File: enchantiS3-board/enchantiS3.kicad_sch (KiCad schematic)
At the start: 61 parts, among them J1 USB_C_Receptacle_USB2.0, SW1 B3U-1000P, SW2 B3U-1000P, U1 USBLC6-2P6, U11 MAX17262REWL+T, U12 BQ25185DLHR, U13 ICM-42670-P, U2 MMC5633NJL, U4 NCP167AMX330TBG, U9 NCP167AMX330TBG

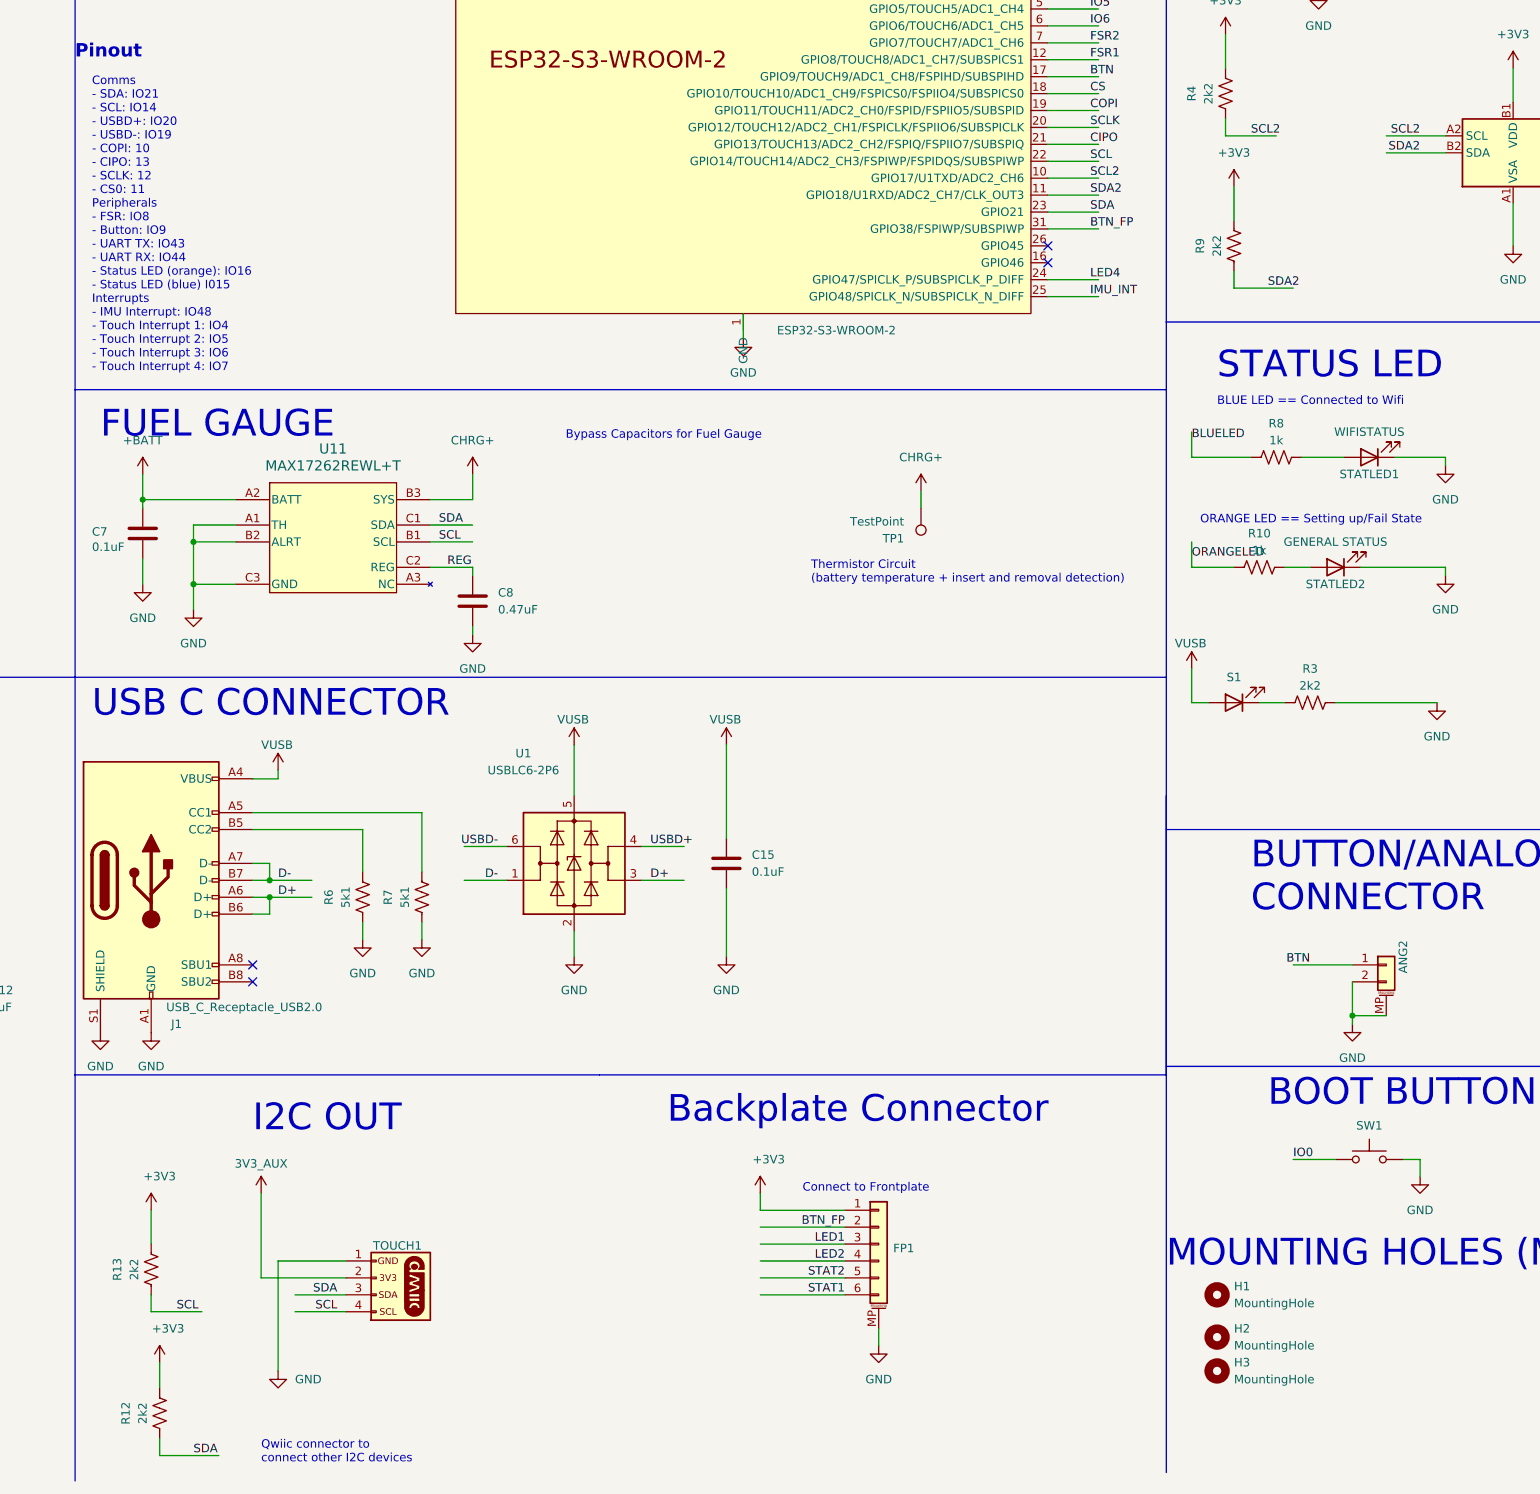
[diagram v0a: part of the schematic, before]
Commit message: fixed hole size constraints for pcbway manufacturing, updated frontplate connector,
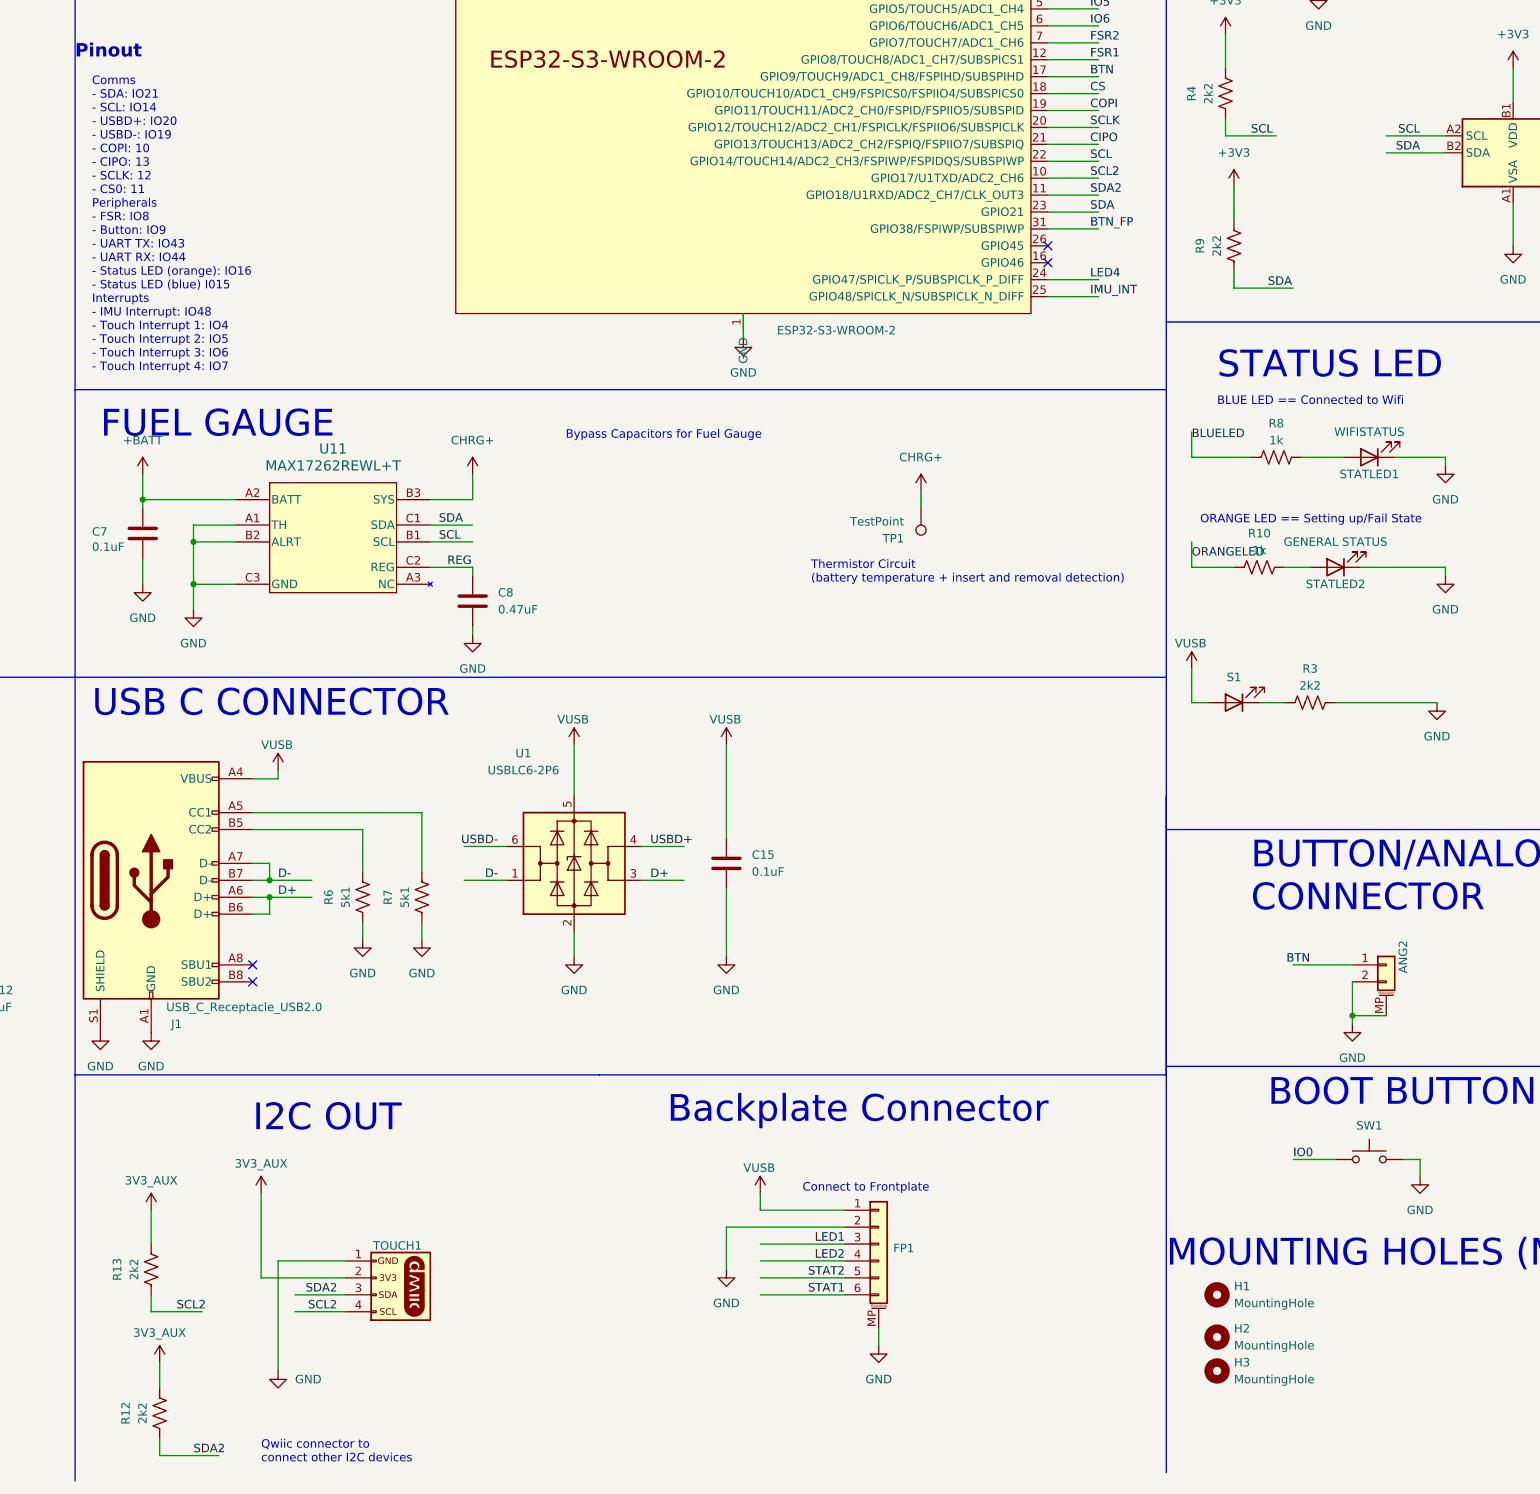
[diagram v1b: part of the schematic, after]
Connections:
- net +3V3: no longer FP1.1 (Pin_1), R12.2, R13.2
- net 3V3_AUX: now also R12.2, R13.2
- net BTN_FP: no longer FP1.2 (Pin_2)
- net GND: now also FP1.2 (Pin_2)
- net SCL: now also R4.1, U2.A2 (SCL); no longer R13.1, TOUCH1.4 (SCL)
- net SCL2: now also R13.1, TOUCH1.4 (SCL); no longer R4.1, U2.A2 (SCL)
- net SDA: now also R9.1, U2.B2 (SDA); no longer R12.1, TOUCH1.3 (SDA)
- net SDA2: now also R12.1, TOUCH1.3 (SDA); no longer R9.1, U2.B2 (SDA)
- net VUSB: now also FP1.1 (Pin_1)

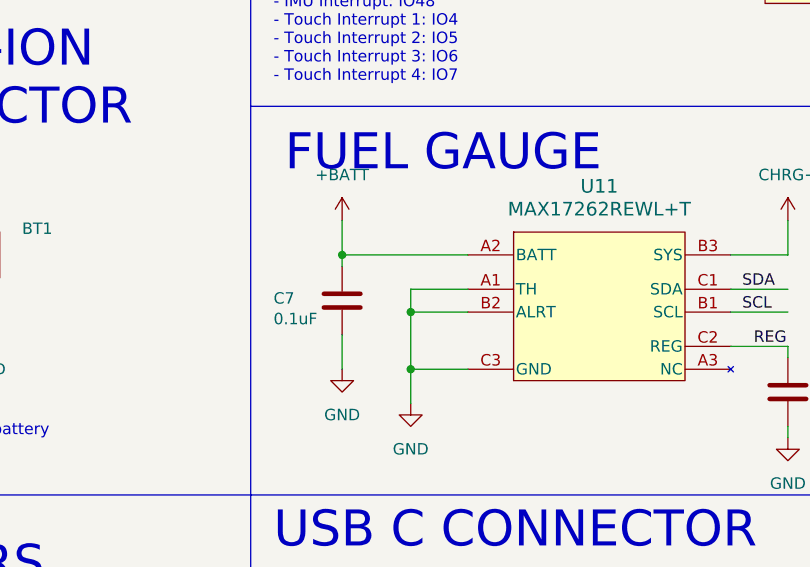
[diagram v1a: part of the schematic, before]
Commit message: add sensor fusion testing firmware
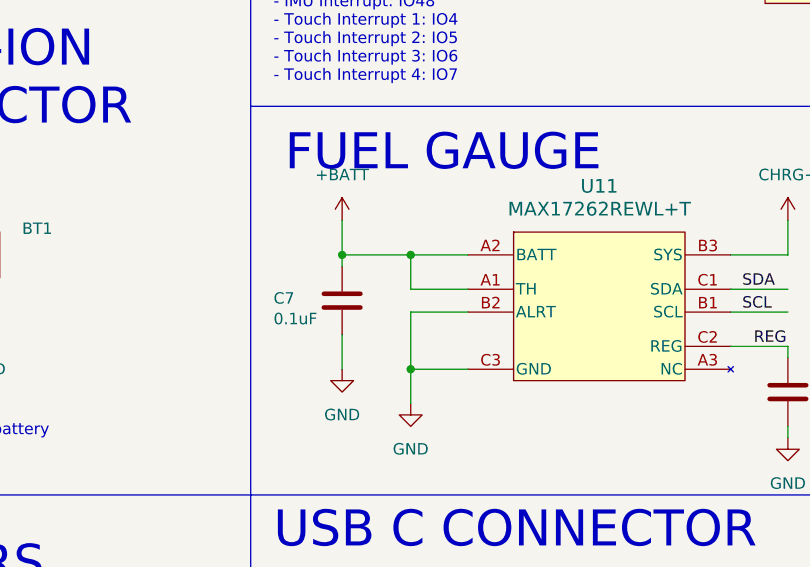
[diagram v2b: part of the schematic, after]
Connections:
- net +BATT: now also U11.A1 (TH)
- net GND: no longer U11.A1 (TH)
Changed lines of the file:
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@@
+	)
+	(junction
+		(at 128.27 137.16)
+		(diameter 0)
+		(color 0 0 0 0)
 	)
 	(junction
 		(at 368.3 214.63)
-		(diameter 0)
-		(color 0 0 0 0)
-	)
-	(junction
-		(at 128.27 143.51)
 		(diameter 0)
 		(color 0 0 0 0)
@@
 	(wire
 		(pts
-			(xy 128.27 140.97) (xy 128.27 143.51)
-		)
-		(stroke
-			(width 0)
-			(type default)
-		)
-	)
-	(wire
-		(pts
 			(xy 391.16 204.47) (xy 392.43 204.47)
 		)
@@
 	(wire
 		(pts
+			(xy 128.27 137.16) (xy 120.65 137.16)
+		)
+		(stroke
+			(width 0)
+			(type default)
+		)
+	)
+	(wire
+		(pts
 			(xy 278.13 127) (xy 278.13 130.81)
 		)
@@
 	(wire
 		(pts
+			(xy 128.27 140.97) (xy 128.27 137.16)
+		)
+		(stroke
+			(width 0)
+			(type default)
+		)
+	)
+	(wire
+		(pts
 			(xy 391.16 214.63) (xy 397.51 214.63)
 		)
@@
 	(wire
 		(pts
-			(xy 134.62 137.16) (xy 120.65 137.16)
+			(xy 134.62 137.16) (xy 128.27 137.16)
 		)
 		(stroke
@@
 	(wire
 		(pts
-			(xy 128.27 140.97) (xy 134.62 140.97)
-		)
-		(stroke
-			(width 0)
-			(type default)
-		)
-	)
-	(wire
-		(pts
 			(xy 123.19 278.13) (xy 123.19 280.67)
 		)
 		(stroke
+			(width 0)
+			(type default)
+		)
+	)
+	(wire
+		(pts
+			(xy 134.62 140.97) (xy 128.27 140.97)
+		)
+		(stroke

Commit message: added capsense controller on enchantiS3 board
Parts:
- removed ANG2: CONN HEADER SMD 2POS 1MM, ENCHANTI_connectors:Molex_Pico-Clasp_2pin_Vertical, symbol ENCHANTI_connectors:PicoClasp_2pin
- removed BOARDLAYOUT1: LAYOUT, pin-layout:board-layout, symbol pin-layout:board-layout
- removed CHARGLED1: S1, LED_SMD:LED_0402_1005Metric, symbol Device:LED
- removed FP1: CONN HEADER SMD 6POS 1MM, ENCHANTI_connectors:Molex_Pico-Clasp_501331-0607_1x06-1MP_P1.00mm_Vertical, symbol Connector_Generic_MountingPin:Conn_01x06_MountingPin
- removed R10: 1k, Resistor_SMD:R_0402_1005Metric, symbol Device:R_US
- removed R3, R4, R9: 2k2, Resistor_SMD:R_0402_1005Metric, symbol Device:R_US
- removed STATLED1: WIFISTATUS, LED_SMD:LED_0402_1005Metric, symbol Device:LED
- removed STATLED2: GENERAL STATUS, LED_SMD:LED_0402_1005Metric, symbol Device:LED
- removed SW1, SW2: B3U-1000P, Button_Switch_SMD:SW_SPST_B3U-1000P, symbol Switch:SW_Push
- removed SYS2: SYS, symbol power-symbols:VSYS
- removed U11: MAX17262REWL+T, ENCHANTI_battery-management:MAX17262, symbol ENCHANTI_battery-management:MAX17262REWL+T
- removed U2: MMC5633NJL, Package_BGA:WLP-4_0.86x0.86mm_P0.4mm, symbol Sensor_Magnetic:MMC5633NJL
- added C10, C26, C59: 1uF, Capacitor_SMD:C_0402_1005Metric, symbol Device:C
- added C14, C27, C6, C61, C66: 0.1uF, Capacitor_SMD:C_0402_1005Metric, symbol Device:C
- added C16, C20, C24, C25: 2.2nF, Capacitor_SMD:C_0402_1005Metric, symbol Device:C
- added CHARGLED2: RED_LED, LED_SMD:LED_0603_1608Metric, symbol Device:LED
- added CHARGLED3: YELLOW_LED, LED_SMD:LED_0603_1608Metric, symbol Device:LED
- added D2: NUP2105L, Package_TO_SOT_SMD:SOT-23, symbol Power_Protection:NUP2105L
- added FP1: CONN HEADER SMD 6POS 1MM, Connector_Molex:Molex_Pico-Clasp_501331-0607_1x06-1MP_P1.00mm_Vertical, symbol ENCHANTI_connectors:PicoClasp_6pin
- added J2: Programming Header, ENCHANTI_connectors:SAMTEC_FTSH-105-01-F-DV-P-TR, symbol ENCHANTI_connectors:Programming_Header
- added R14, R16: 2k2, Resistor_SMD:R_0402_1005Metric, symbol Device:R_US
- added R19: 120, Resistor_SMD:R_0402_1005Metric, symbol Device:R_US
- added R3: 5mOhm, ENCHANTI_resistors:WSTC080R003_20, symbol ENCHANTI_resistors:WSTC0805DLR005FNR
- added R42, R43: 604R, Resistor_SMD:R_0402_1005Metric, symbol Device:R_US
- added R50: 261, Resistor_SMD:R_0402_1005Metric, symbol Device:R_US
- added R51: 549, Resistor_SMD:R_0402_1005Metric, symbol Device:R_US
- added SW1, SW2, SW3: PTS810, ENCHANTI_switches:SW_SPST_PTS810, symbol ENCHANTI_switches:PTS810
- added TOUCH2: FFCHEADER, ffc_footprints:CON_541323262_MOL, symbol Connector_Generic_MountingPin:Conn_01x32_MountingPin
- added TP11: TestPoint, TestPoint:TestPoint_Pad_D1.0mm, symbol Connector:TestPoint
- added U14: MAX17260SETD+T, ENCHANTI_battery-management:TDFN-14-EP-ADI, symbol ENCHANTI_battery-management:MAX17260SETD+T
- added U5: CY8C4149, TQFP50P1200X1200X160-64N:TQFP50P1200X1200X160-64N, symbol CY8C414X_TQFP64:CY8C414X_TQFP64
- added U8: TCAN3413DRBR, ENCHANTI_transceivers:VSON8-DRB_TEX, symbol ENCHANTI_transceivers:TCAN3413DRBR
- added USER_LED1: ORANGE_LED, LED_SMD:LED_0603_1608Metric, symbol Device:LED
- added USER_LED2: BLUE_LED, LED_SMD:LED_0603_1608Metric, symbol Device:LED
- C31: renamed from C7; mpn CL05B104KO5NNNC -> (none)
- C46: renamed from C8; mpn GRT155R61C474KE01D -> (none)
- CANFD1: renamed from TOUCH1; mpn BM04B-SRSS-TB -> (none)
- R8: value 1k -> 10k; Mfg Part # ERJ-2RKF1001X -> ERJ-2RKF1002X; mpn ERJ-2RKF1001X -> ERJ-2RKF1002X
- renumbered TP1 to TP3
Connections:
- net IO6 is gone; now on net BTN_FP: MCU1.6 (GPIO6/TOUCH6/ADC1_CH5)
- net +3V3: now also FP1.3 (Pin_3), SW3.2; no longer C17.1, C18.1, C3.1, U13.5 (VDDIO), U13.8 (VDD)
- net +BATT: now also R3.1, U14.1 (TH), U14.6 (BATT)
- net 3V3_AUX: now also C10.2, C14.2, C26.2, C6.2, J2.1 (VDD), R14.2, R16.2, U5.26 (VDDD_1), U5.50 (VDDD_2), U5.56 (VDDA)
- net BLUELED: now also R51.1; no longer R8.1
- net CHRG+: now also R3.2
- net EN: now also SW2.1
- net GND: now also R8.1, C10.1, C14.1, C16.1, C20.1, C24.1, C25.1, C26.1, C27.1, C59.2, C6.1, C61.2, C66.2, D2.3 (A), FP1.1 (Pin_1), FP1.MP (MountPin), J2.3 (GND), J2.5 (GND), J2.7 (NC), J2.9 (GND), SW1.2, SW2.2, TOUCH2.1 (Pin_1), TOUCH2.32 (Pin_32), TOUCH2.MP (MountPin), TP11.1, U14.12 (ALRT), U14.15 (EPAD), U14.8 (GND), U14.9 (CSPL), U5.10 (VSSD_1), U5.17 (VSSD_2), U5.49 (VSSD_3), U5.57 (VSSA), U8.2 (GND), U8.9 (EPAD)
- net IO0: now also SW1.1
- net ORANGELED: now also R50.1
- net REG: now also U14.11 (REG)
- net SCL: now also R14.1, U14.14 (SCL)
- net SCL2: now also FP1.5 (Pin_5)
- net SDA: now also R16.1, U14.13 (SDA)
- net SDA2: now also FP1.4 (Pin_4)
- net STAT1: now also R42.2
- net STAT2: now also R43.2
- net VUSB: now also CHARGLED2.2 (A), CHARGLED3.2 (A)
- net USER_BTN: now reaches R8.2
- net USER_BTN: now also SW3.1
- net LED1 renamed TOUCH_COPI
- net TOUCH_COPI: now also U5.43 (P0_4)
- net LED2 renamed TOUCH_CIPO
- net TOUCH_CIPO: now also U5.44 (P0_5)
- net LED3 renamed TOUCH_SCLK
- net TOUCH_SCLK: now also U5.45 (P0_6)
- net LED4 renamed TOUCH_CS
- net TOUCH_CS: now also U5.46 (P0_7)
- new net: R51.2, USER_LED2.1 (K)
- new net: R50.2, USER_LED1.1 (K)
- new net: CHARGLED2.1 (K), R42.1
- new net: CHARGLED3.1 (K), R43.1
- new net: CANFD1.NC1 (NC), CANFD1.NC2 (NC)
- new net +3V3_AUX: C17.1, C18.1, C3.1, C59.1, C61.1, C66.1, CANFD1.2 (3v3), FP1.2 (Pin_2), U13.5 (VDDIO), U13.8 (VDD), U8.3 (VCC), U8.5 (VIO), USER_LED1.2 (A), USER_LED2.2 (A)
- new net BUTTON_FP: FP1.6 (Pin_6)
- new net CANFD_RX: U5.41 (P0_2)
- new net CANFD_TX: U5.42 (P0_3)
- new net CAN_H: CANFD1.3 (SDA), D2.2 (K), R19.2, U8.7 (CANH)
- new net CAN_L: CANFD1.4 (SCL), D2.1 (K), R19.1, U8.6 (CANL)
- new net CAN_MODE: U8.8 (STB)
- new net CMOD00: C16.2, U5.29 (P4_2)
- new net CMOD01: C20.2, U5.30 (P4_3)
- new net CMOD10: C24.2, U5.37 (P7_0)
- new net CMOD11: C25.2, U5.38 (P7_1)
- new net CSN: R3.3 (CSN), U14.7 (CSN)
- new net CSPH: R3.4 (CSP), U14.10 (CSPH)
- new net FDCAN1_RX: U8.4 (RXD)
- new net FDCAN1_TX: U8.1 (TXD)
- new net MSC000: TOUCH2.2 (Pin_2), U5.58 (P1_0)
- new net MSC001: TOUCH2.3 (Pin_3), U5.59 (P1_1)
- new net MSC002: TOUCH2.4 (Pin_4), U5.60 (P1_2)
- new net MSC003: TOUCH2.5 (Pin_5), U5.61 (P1_3)
- new net MSC004: TOUCH2.6 (Pin_6), U5.62 (P1_4)
- new net MSC005: TOUCH2.7 (Pin_7), U5.63 (P1_5)
- new net MSC006: TOUCH2.8 (Pin_8), U5.64 (P1_6)
- new net MSC007: TOUCH2.16 (Pin_16), U5.1 (P1_7)
- new net MSC008: TOUCH2.17 (Pin_17), U5.2 (P2_0)
- new net MSC009: TOUCH2.18 (Pin_18), U5.3 (P2_1)
- new net MSC010: TOUCH2.19 (Pin_19), U5.4 (P2_2)
- new net MSC011: TOUCH2.20 (Pin_20), U5.5 (P2_3)
- new net MSC012: TOUCH2.21 (Pin_21), U5.6 (P2_4)
- new net MSC013: TOUCH2.22 (Pin_22), U5.7 (P2_5)
- new net MSC014: TOUCH2.23 (Pin_23), U5.8 (P2_6)
- new net MSC015: TOUCH2.24 (Pin_24), U5.9 (P2_7)
- new net MSC022: TOUCH2.25 (Pin_25), U5.12 (P6_0)
- new net MSC023: TOUCH2.26 (Pin_26), U5.13 (P6_1)
- new net MSC024: TOUCH2.27 (Pin_27), U5.14 (P6_2)
- new net MSC026: TOUCH2.28 (Pin_28), U5.15 (P6_4)
- new net MSC029: TOUCH2.29 (Pin_29), U5.16 (P6_5)
- new net MSC030: TOUCH2.31 (Pin_31), U5.18 (P3_0)
- new net MSC031: TOUCH2.30 (Pin_30), U5.19 (P3_1)
- new net MSC034: U5.22 (P3_4)
- new net MSC035: U5.23 (P3_5)
- new net MSC036: U5.24 (P3_6)
- new net MSC037: U5.25 (P3_7)
- new net MSC048: U5.31 (P4_4)
- new net MSC049: U5.32 (P4_5)
- new net MSC050: U5.33 (P4_6)
- new net MSC051: U5.34 (P4_7)
- new net MSC100: U5.35 (P5_6)
- new net MSC101: TOUCH2.9 (Pin_9), U5.55 (P5_5)
- new net MSC102: TOUCH2.10 (Pin_10), U5.54 (P5_3)
- new net MSC103: TOUCH2.11 (Pin_11), U5.53 (P5_2)
- new net MSC105: U5.36 (P5_7)
- new net MSC114: TOUCH2.15 (Pin_15), U5.39 (P0_0)
- new net MSC115: TOUCH2.14 (Pin_14), U5.40 (P0_1)
- new net MSC130: TOUCH2.13 (Pin_13), U5.51 (P5_0)
- new net MSC131: TOUCH2.12 (Pin_12), U5.52 (P5_1)
- new net RES: J2.10 (RES), U5.47 (~{XRES})
- new net SWCLK: J2.4 (SWCLK), U5.21 (P3_3)
- new net SWDA: J2.2 (SWDIO), U5.20 (P3_2)
- new net VCCD: C27.2, U5.48 (VCCD)
- no-connect marks 6 -> 11
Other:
- note added: "CAN TRANSCEIVER"
- note added: "CAPSENSE SENSOR"
- note added: "CONNECTORS"
- note added: "Connector for Front plate"
- note added: "ESD Protection"
- note added: "General LEDs for board status"
- note added: "I2C Pullups"
- note added: "LED For Battery charging status, Table 8.2 in BQ25185 datasheet for outputs"
- note added: "Programming Header for 10 pin Ribbon Cable"
- note added: "Qwiic connector to connect CANFD boards together"
- note added: "Touch Capacitors"
- note removed: "BLUE LED == Connected to Wifi"
- note removed: "BOARD LAYOUT"
- note removed: "BOOT BUTTON"
- note removed: "BUTTON/ANALOG CONNECTOR"
- note removed: "Backplate Connector"
- note removed: "Bypass Capacitors for Fuel Gauge"
- note removed: "Connect to Frontplate"
- note removed: "FSR CONNECTOR"
- note removed: "I2C OUT"
- note removed: "LIPO/LI-ION CONNECTOR"
- note removed: "ORANGE LED == Setting up/Fail State"
- note removed: "RESET BUTTON"
- note removed: "Test point for current measurement"
- note removed: "Thermistor Circuit (battery temperature + insert and removal detection)"
- moved on the sheet: ANG1, ANG3, BT1, C11, C12, C15, C17, C18, C21, C22, C23, C3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
